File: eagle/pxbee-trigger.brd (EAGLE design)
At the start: 61.7 x 96.4 mm, 21 parts, among them J1 5452153, J2 1963599, K1 APAN3103, K2 APAN3103, K3 APAN3103, K4 APAN3103, Q1 BC548BTA, Q2 BC548BTA, Q3 BC548BTA, Q4 BC548BTA

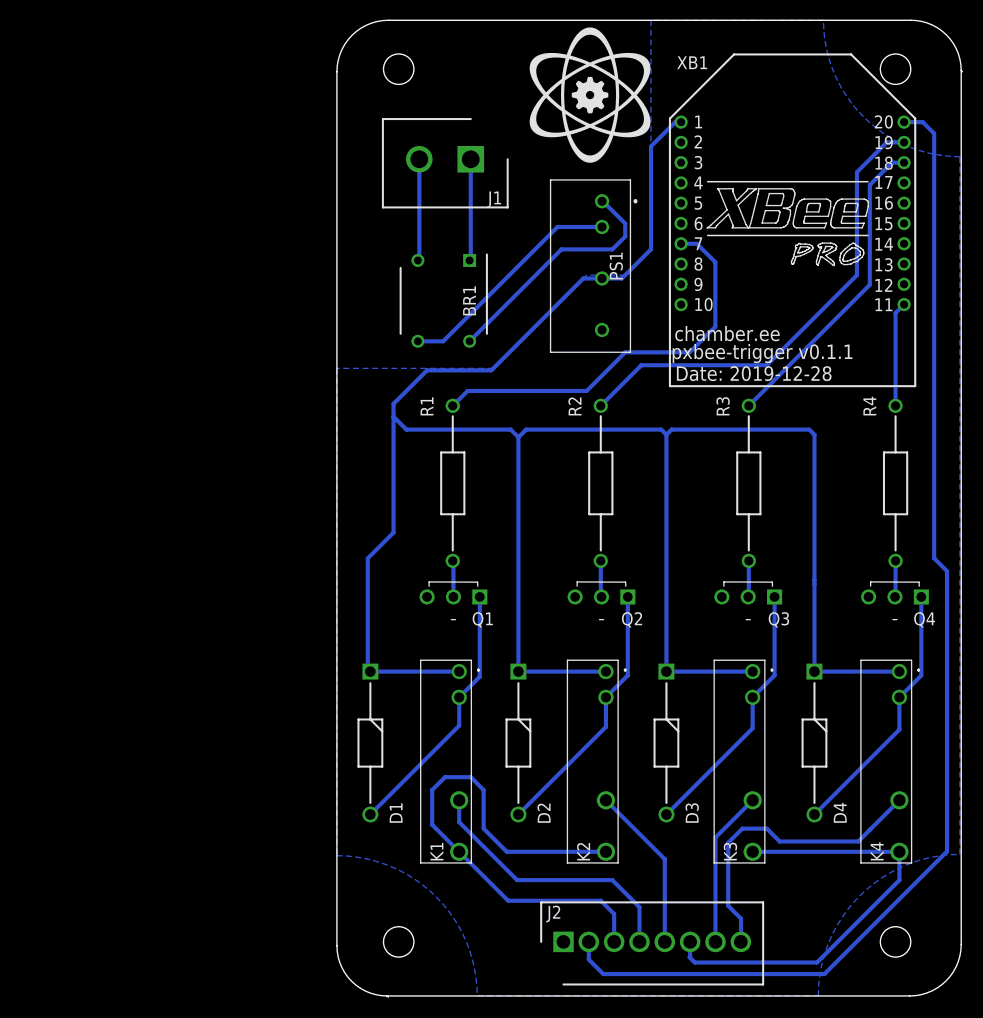
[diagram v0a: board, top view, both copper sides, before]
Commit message: Change of connector elements, smaller dimensions
- Change from Phoenix contact to 3.5mm step Molex Eurotype connectors
- Dimension the board to fit inside a small plastic conjunction box 75x75mm
- Still work in progress (WIP)
- Addresses fabrication remarks in #5
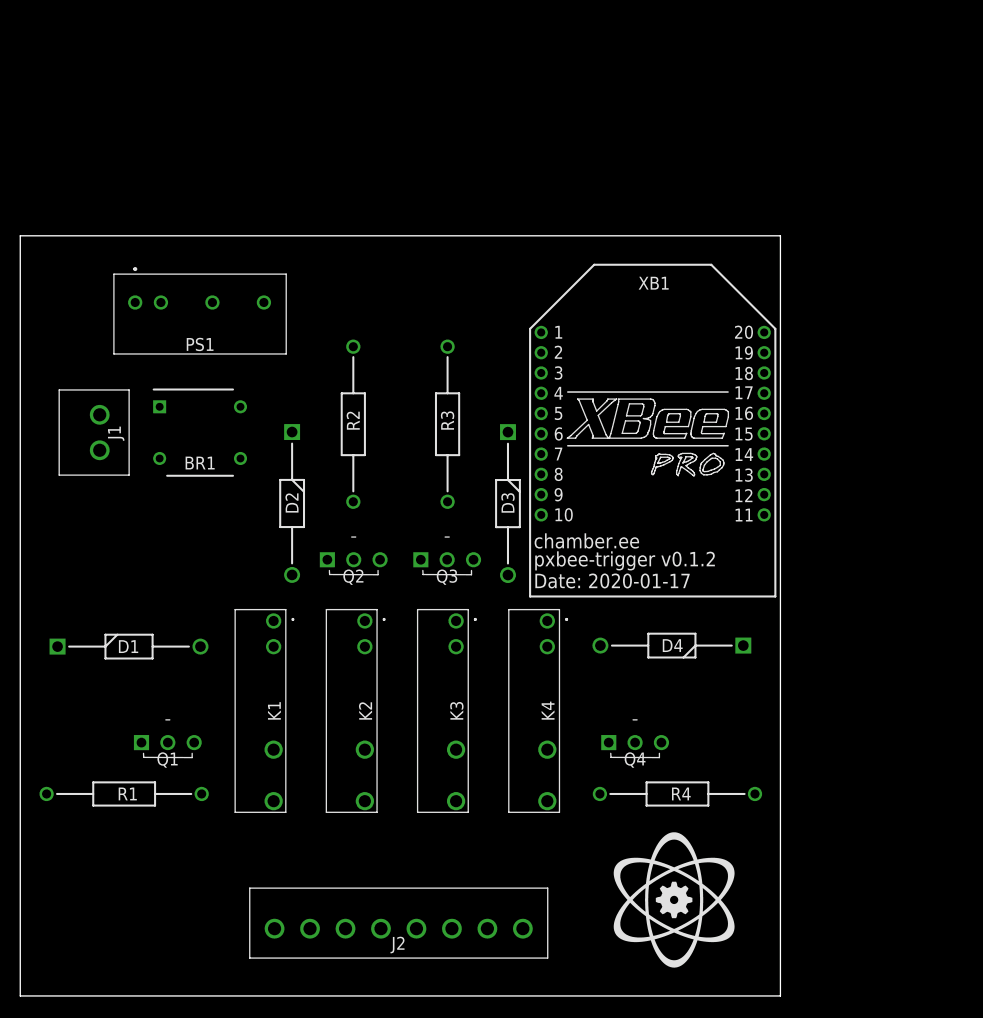
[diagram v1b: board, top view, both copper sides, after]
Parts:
- J1: value 5452153 -> 39501-1002; device parts:SHDR2W110P0X508_1X2_1216X857X1 -> parts:395011002
- J2: value 1963599 -> 39501-1008; device parts:SHDR8W80P0X250_1X8_2190X810X10 -> parts:395011008
- moved J1 46.5 mm to (7.84, 53.8), turned to 90 degrees
- moved R1 46.2 mm to (2.60, 19.9), turned to 0 degrees
- moved PS1 38.8 mm to (17.7, 67.3), turned to 0 degrees
- moved R4 37.1 mm to (57.2, 19.9), turned to 0 degrees
- moved Q1 36.3 mm to (12.0, 25.0), turned to 0 degrees
- moved K4 35.1 mm to (52.0, 37.0)
- moved Q3 35.1 mm to (39.5, 43.0), turned to 0 degrees
- moved Q4 34.0 mm to (58.1, 25.0), turned to 0 degrees
- moved D2 32.5 mm to (26.8, 55.6)
- moved D1 31.0 mm to (3.68, 34.5), turned to 0 degrees
- moved R3 30.3 mm to (42.2, 48.8)
- moved Q2 29.9 mm to (30.3, 43.0), turned to 0 degrees
- moved K3 29.7 mm to (43.0, 37.0)
- moved J2 28.5 mm to (25.1, 6.64)
- moved D3 28.3 mm to (48.1, 55.6)
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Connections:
- net N$8: now also J1.2; no longer J1.1
- net N$9: now also J1.1; no longer J1.2
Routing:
- net VCC: track 220.9 -> 0.00 mm
- net DIO0: track 117.5 -> 0.00 mm
- net COM1: track 50.7 -> 0.00 mm
- net N$14: track 46.6 -> 0.00 mm
- net COM2: track 43.1 -> 0.00 mm
- net N$13: track 39.6 -> 0.00 mm
- net N$15: track 31.0 -> 0.00 mm
- net ACT4: track 30.0 -> 0.00 mm
- net ACT1: track 26.8 -> 0.00 mm
- net N$4: track 25.9 -> 0.00 mm
- net N$3: track 25.9 -> 0.00 mm
- net N$6: track 25.9 -> 0.00 mm
- net N$12: track 25.8 -> 0.00 mm
- net N$10: track 24.1 -> 0.00 mm
- net N$11: track 22.8 -> 0.00 mm
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- removed copper zone on layer 16, net GND
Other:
- board size 61.7 x 96.4 mm -> 75 x 75 mm
- board text added: "Date: 2020-01-17"
- board text added: "pxbee-trigger v0.1.2"
- board text removed: "Date: 2019-12-28"
- board text removed: "pxbee-trigger v0.1.1"

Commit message: Board routed; Updated parts library
- Freed pin 20, using pin 4 for gate/door status input
- Addresses findings in #5
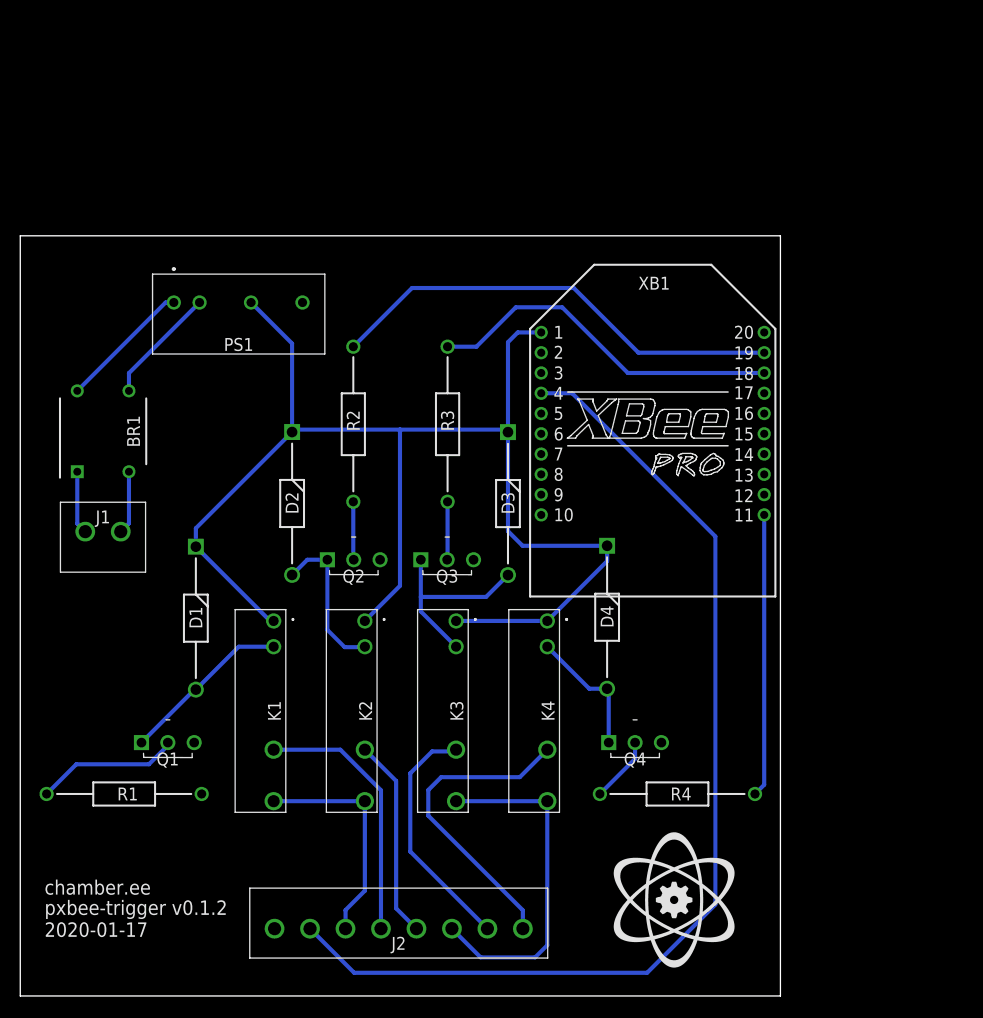
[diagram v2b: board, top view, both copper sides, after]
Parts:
- moved D1 16.8 mm to (17.3, 44.3), turned to 270 degrees
- moved D4 16.7 mm to (57.9, 44.4), turned to 270 degrees
- moved BR1 9.57 mm to (8.17, 55.7), turned to 90 degrees
- moved J1 8.29 mm to (9.91, 45.8), turned to 180 degrees
- moved PS1 3.81 mm to (21.6, 67.3)
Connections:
- removed net DIO0: J2.2, XB1.20
- new net DIO12: J2.2, XB1.4
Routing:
- net VCC: track 0.00 -> 133.7 mm
- net DIO12: track 0.00 -> 103.9 mm
- net N$14: track 0.00 -> 45.6 mm
- net N$15: track 0.00 -> 35.5 mm
- net COM2: track 0.00 -> 34.3 mm
- net ACT4: track 0.00 -> 30.9 mm
- net N$16: track 0.00 -> 27.9 mm
- net ACT1: track 0.00 -> 25.9 mm
- net ACT3: track 0.00 -> 24.0 mm
- net COM1: track 0.00 -> 22.4 mm
- net ACT2: track 0.00 -> 19.8 mm
- net N$6: track 0.00 -> 19.5 mm
- net N$3: track 0.00 -> 17.0 mm
- net N$4: track 0.00 -> 15.4 mm
- net N$1: track 0.00 -> 14.2 mm
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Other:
- board text added: "2020-01-17"
- board text removed: "Date: 2020-01-17"

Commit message: One airwire network detected; brd corners chopped
- Addresses findings in #5
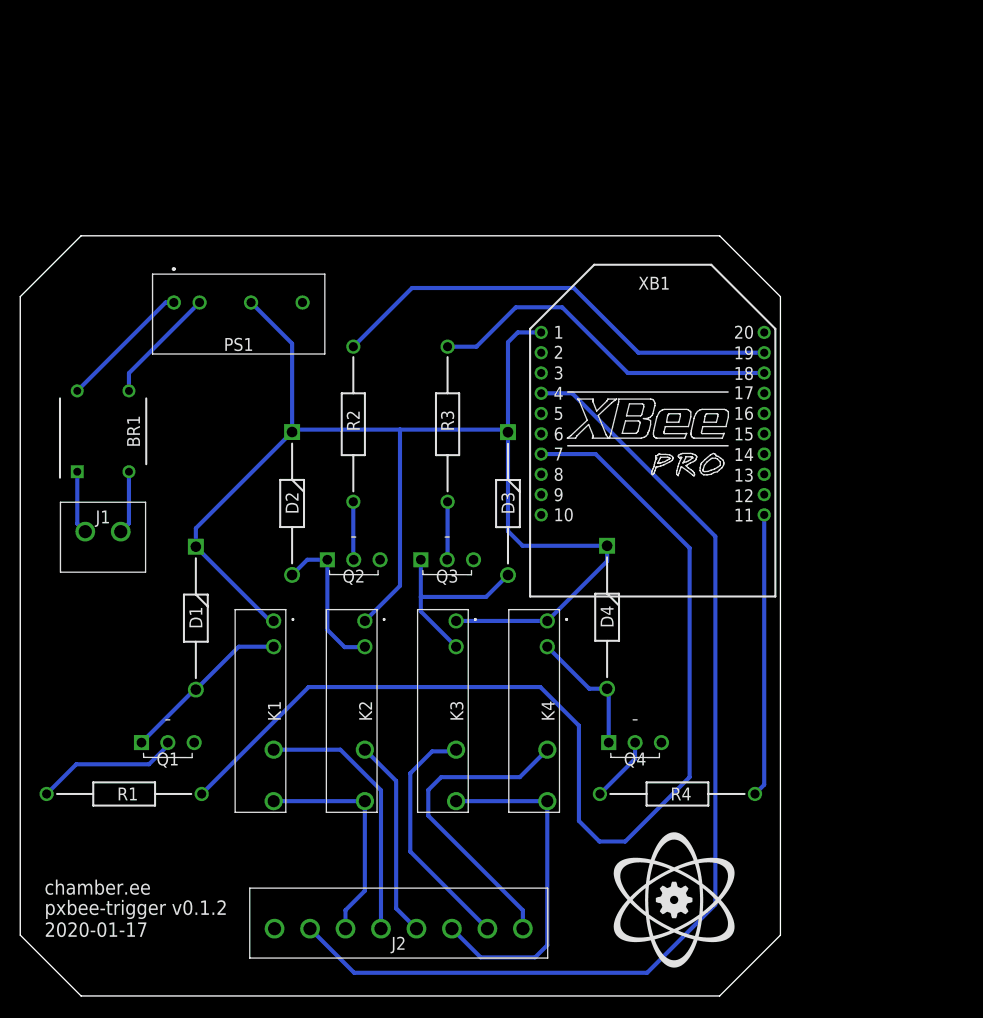
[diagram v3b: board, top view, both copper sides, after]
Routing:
- net N$13: track 0.00 -> 108.0 mm
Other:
- outline, holes or cut-outs redrawn
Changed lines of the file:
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@@
 <setting verticaltext="up"/>
 </settings>
-<grid distance="1" unitdist="mm" unit="mm" style="lines" multiple="1" display="yes" altdistance="0.1" altunitdist="mm" altunit="mm"/>
+<grid distance="50" unitdist="mil" unit="mil" style="lines" multiple="1" display="yes" altdistance="5" altunitdist="mil" altunit="mil"/>
 <layers>
 <layer number="1" name="Top" color="4" fill="1" visible="yes" active="yes"/>
@@
 <board>
 <plain>
-<wire x1="0" y1="0" x2="75" y2="0" width="0" layer="20"/>
-<wire x1="75" y1="0" x2="75" y2="75" width="0" layer="20"/>
-<wire x1="75" y1="75" x2="0" y2="75" width="0" layer="20"/>
-<wire x1="0" y1="75" x2="0" y2="0" width="0" layer="20"/>
+<wire x1="6" y1="0" x2="69" y2="0" width="0" layer="20"/>
+<wire x1="75" y1="6" x2="75" y2="69" width="0" layer="20"/>
+<wire x1="69" y1="75" x2="6" y2="75" width="0" layer="20"/>
 <text x="2.39" y="10" size="1.4224" layer="21" rot="R180" align="top-right">chamber.ee</text>
 <text x="2.39" y="8" size="1.4224" layer="21" rot="R180" align="top-right">pxbee-trigger v0.1.2</text>
@@
 <rectangle x1="64.319209375" y1="16.13245625" x2="64.707828125" y2="16.1408375" layer="21"/>
 <rectangle x1="64.385246875" y1="16.1408375" x2="64.649409375" y2="16.14921875" layer="21"/>
+<wire x1="0" y1="69" x2="0" y2="6" width="0" layer="20"/>
+<wire x1="75" y1="69" x2="69" y2="75" width="0" layer="20"/>
+<wire x1="6" y1="75" x2="0" y2="69" width="0" layer="20"/>
+<wire x1="0" y1="6" x2="6" y2="0" width="0" layer="20"/>
+<wire x1="69" y1="0" x2="75" y2="6" width="0" layer="20"/>
 </plain>
 <attributes>
@@
 <contactref element="R1" pad="2"/>
 <contactref element="XB1" pad="7"/>
-<wire x1="17.9" y1="19.93" x2="51.4" y2="53.466" width="0" layer="19" extent="1-1"/>
+<wire x1="17.9" y1="19.93" x2="28.45" y2="30.48" width="0.4064" layer="16"/>
+<wire x1="51.308" y1="30.48" x2="55.118" y2="26.67" width="0.4064" layer="16"/>
+<wire x1="55.118" y1="26.67" x2="55.118" y2="17.272" width="0.4064" layer="16"/>
+<wire x1="55.118" y1="17.272" x2="57.15" y2="15.24" width="0.4064" layer="16"/>
+<wire x1="57.15" y1="15.24" x2="59.69" y2="15.24" width="0.4064" layer="16"/>
+<wire x1="59.69" y1="15.24" x2="66.04" y2="21.59" width="0.4064" layer="16"/>
+<wire x1="66.04" y1="21.59" x2="66.04" y2="44.196" width="0.4064" layer="16"/>
+<wire x1="66.04" y1="44.196" x2="56.769" y2="53.467" width="0.4064" layer="16"/>
+<wire x1="56.769" y1="53.467" x2="51.401" y2="53.467" width="0.4064" layer="16"/>
+<wire x1="51.401" y1="53.467" x2="51.4" y2="53.466" width="0.4064" layer="16"/>
+<wire x1="28.45" y1="30.48" x2="51.308" y2="30.48" width="0.4064" layer="16"/>
 </signal>
 <signal name="N$14">

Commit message: Board dimension changes
- Dimensioned to 75x75mm
- 9 pin terminal block used to gain one more status pin
- Parts library updated (removed unused parts, added new ones)
- Addresses findings in #5
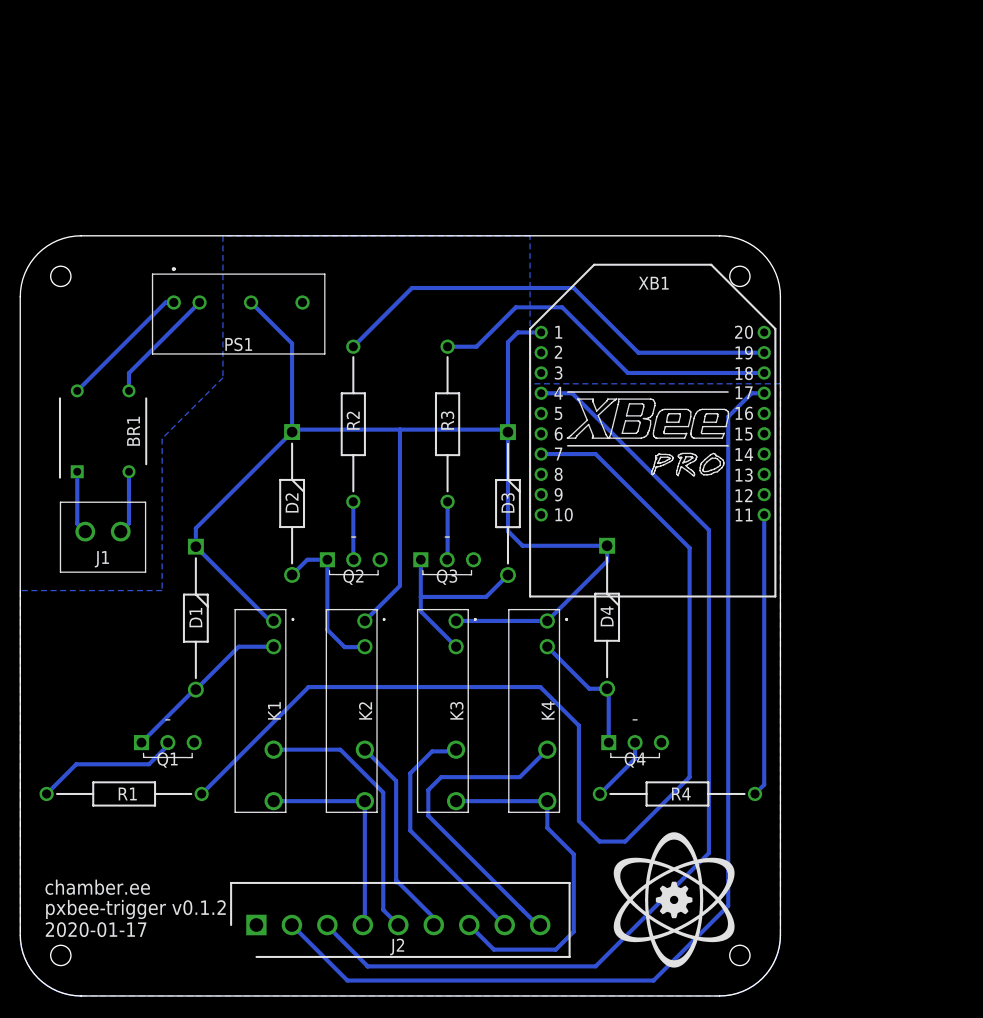
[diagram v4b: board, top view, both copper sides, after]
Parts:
- J2: value 39501-1008 -> 39501-1009; device parts:395011008 -> parts:SHDR9W80P0X350_1X9_3290X690X96
- moved J2 1.83 mm to (23.3, 7.00)
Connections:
- new net DIO3: J2.2, XB1.17
- net ACT1: now also J2.5; no longer J2.4
- net ACT2: now also J2.6; no longer J2.5
- net ACT3: now also J2.8; no longer J2.7
- net ACT4: now also J2.9; no longer J2.8
- net COM1: now also J2.4; no longer J2.3
- net COM2: now also J2.7; no longer J2.6
- net DIO12: now also J2.3; no longer J2.2
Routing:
- net DIO3: track 0.00 -> 101.1 mm
- net DIO12: track 103.9 -> 98.1 mm
- net COM1: track 22.4 -> 21.3 mm
- net COM2: track 34.3 -> 35.0 mm
- net ACT2: track 19.8 -> 20.4 mm
- net ACT4: track 30.9 -> 31.4 mm
- added copper zone on layer 16, net GND
